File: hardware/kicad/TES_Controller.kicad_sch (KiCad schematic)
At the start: 81 parts, among them CN1 B2PS-VH(LF)(SN), CN2 S4B-XH-A(LF)(SN), CN3 DG381-3.5-02P-14-00A(H), CN5 DG381-3.5-02P-14-00A(H), CN6 DG381-3.5-02P-14-00A(H), Q1 AO3400A, Q2 AO3400A, Q3 AO3400A, Q4 AO3401A, U1 ESP32-S3-WROOM-1-N16R8, U10 DG301-5.0-02P-14-00A(H), U12 TJA1051T/3/1J, U5 ADS1115IDGSR, U6 AMS1117-3.3, U8 LMZM23601V5SILR

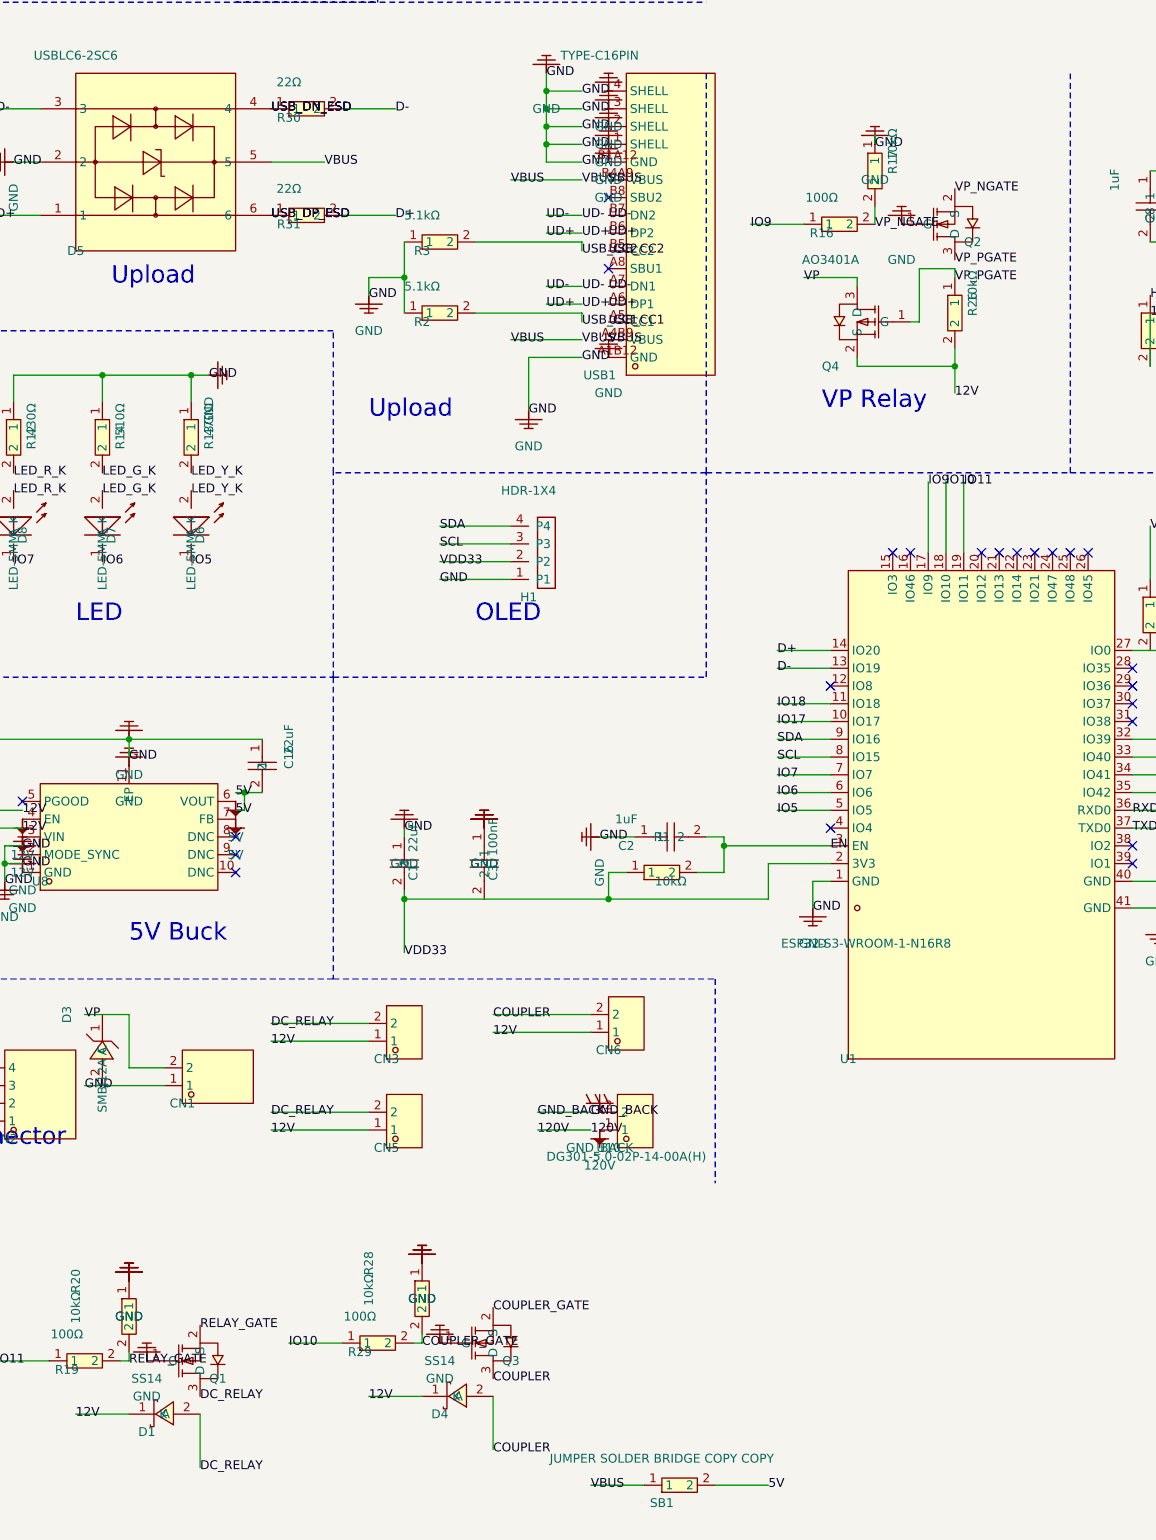
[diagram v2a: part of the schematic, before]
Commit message: Keep the AO3400A pin swap that the EasyEDA design relied on
LCSC's SOT-23-3 footprint for C20917 numbers pads 1 and 2 the opposite
way round from JEDEC TO-236: viewed from the top, 1 -> 2 -> 3 runs
clockwise, so the pad stamped "1" sits under the chip's pin 2. Every
other package in this library runs counter-clockwise, and each of those
checks out against its own datasheet — TJA1051 pin 1 is TXD, AMS1117
pin 1 is GND, USBLC6 pin 2 is GND, and Q4's AO3401A takes its gate on
pad 1 with an unmodified symbol.

The EasyEDA design compensated by drawing Q1-Q3 with a symbol whose
pins 1 and 2 are swapped, which is why the board works. The migration
dropped that: the generated library carries LCSC's own symbol with
pin 1 named G, so the schematic read "gate tied to GND" while the copper
underneath was right. Nothing in ERC or DRC objects to that, and the
failure on a built board is silent — the relay simply never closes.

tools/kicad_lib.py now reapplies the swap after every library
regeneration. The footprint and the PCB are untouched; CLAUDE.md records
the evidence and what the other half of the fix would cost if the
library is ever made to match the datasheet instead.

Side effect worth having: Q1-Q3's pins now line up with the original
drawing, so they keep their wires instead of falling back to labels —
12 components need label-only wiring now rather than 15, and 21 wire
segments are trimmed rather than 31.

Netlist still verifies at zero difference (230 of 230), ERC is clean,
PCB unchanged at 0 DRC errors and 0 unconnected pads.

Co-Authored-By: Claude Opus 5 <noreply@anthropic.com>
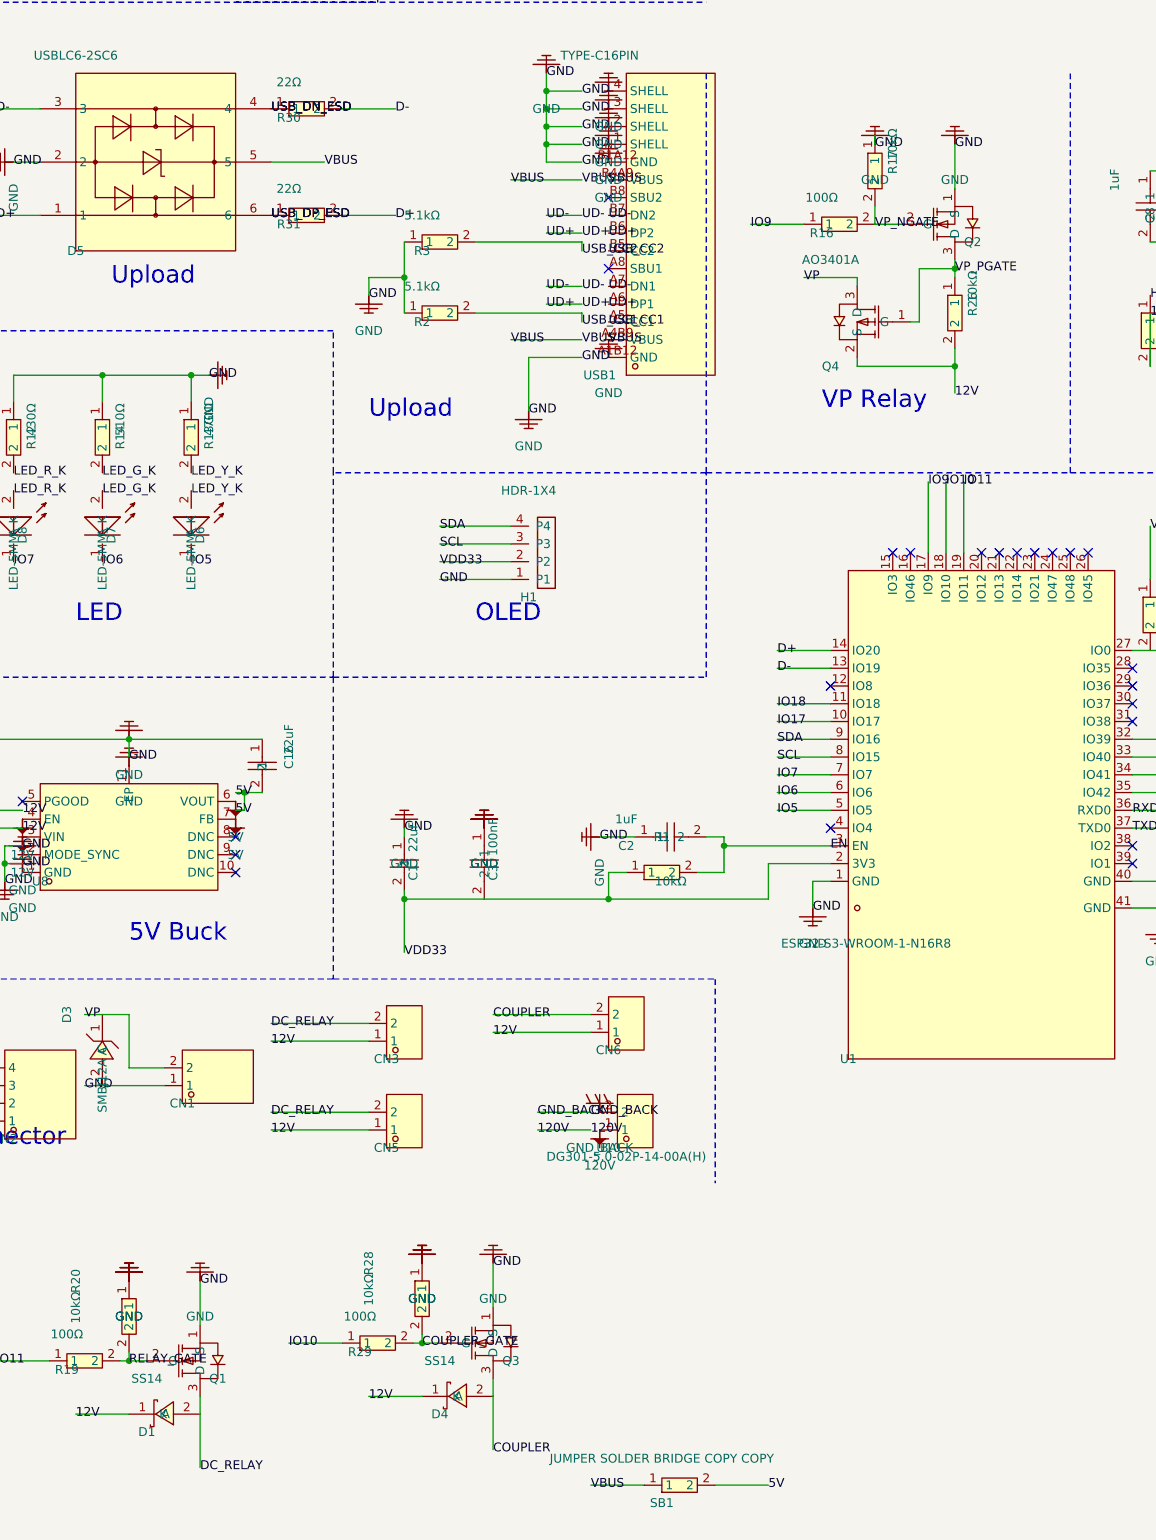
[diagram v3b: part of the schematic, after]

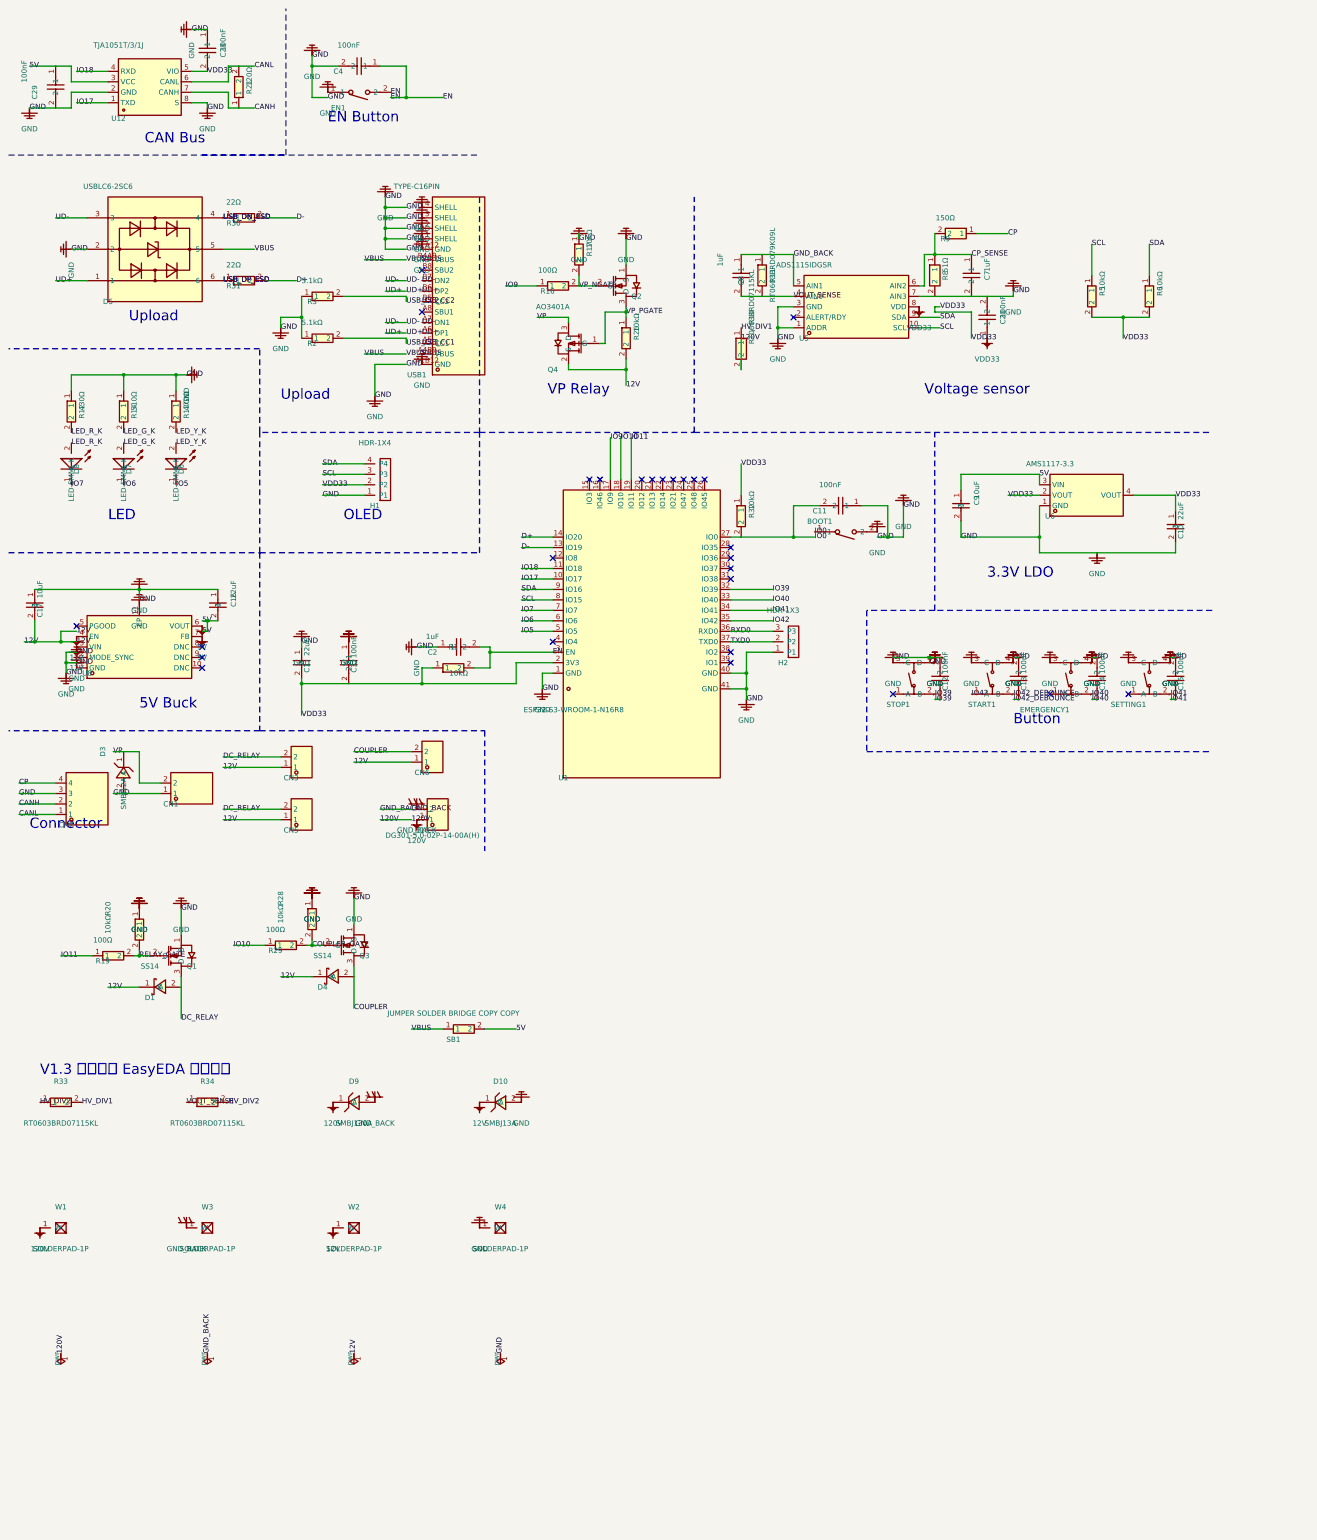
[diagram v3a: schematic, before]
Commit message: Record the V1.3 change set, and pause before it reaches the board
Three changes are decided and carried in the schematic and library; none of
them are on the PCB yet. Recording the split explicitly so the next session
does not mistake it for an unfinished edit:

* U13 24C02S EEPROM (LCSC C18723540) with C30 decoupling — stores the board
  revision so one binary can serve V1.3 and the 30.000-divider units in the
  field. WP to GND, firmware decides when to write.
* D10 becomes SMBJ12A, the part D3 already uses, and moves out from under the
  buck module. Lower clamp (19.9 V against 21.5 V) and no new part number.
* R35, a 10 k that divides Q4's gate drive. Q4 sat at exactly its ±12 V
  absolute-maximum V_GS whenever VP was on, and above it on a 12.6 V rail —
  which matches the field failures: rare, no external damage, fixed by
  replacement. Now −6 V.

The EEPROM cannot reach the PCB yet. Counting tracks and vias rather than only
component courtyards, the nearest free 4×4 mm to an SDA or SCL pad is 31.9 mm,
and 49.3 mm for enough room to escape three pins. Left alone the placer sends
SDA and SCL 28 mm each down the bottom layer, cutting the ground plane the
restructure work created. The board is therefore left at its last good state —
81 footprints, 0 DRC errors, 0 unconnected — rather than half-modified.

Two bugs found while doing this, both fixed and both older than this change:

* easyeda2kicad's --overwrite appends rather than replaces, so every library
  regeneration duplicated every symbol. 35 duplicates removed. The duplicate
  quietly reverted the AO3400A pin renumbering, leaving one symbol with 1=G and
  one with 1=S in the same library.
* The buck-module keepout was the rectangle through the four mounting holes
  rather than the module body, short by 2.4-3.0 mm on every edge. That is how
  D10 came to sit under the module in the first place.

Work stops here pending a decision on patent filing and a possible move to a
private repository. CLAUDE.md now car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
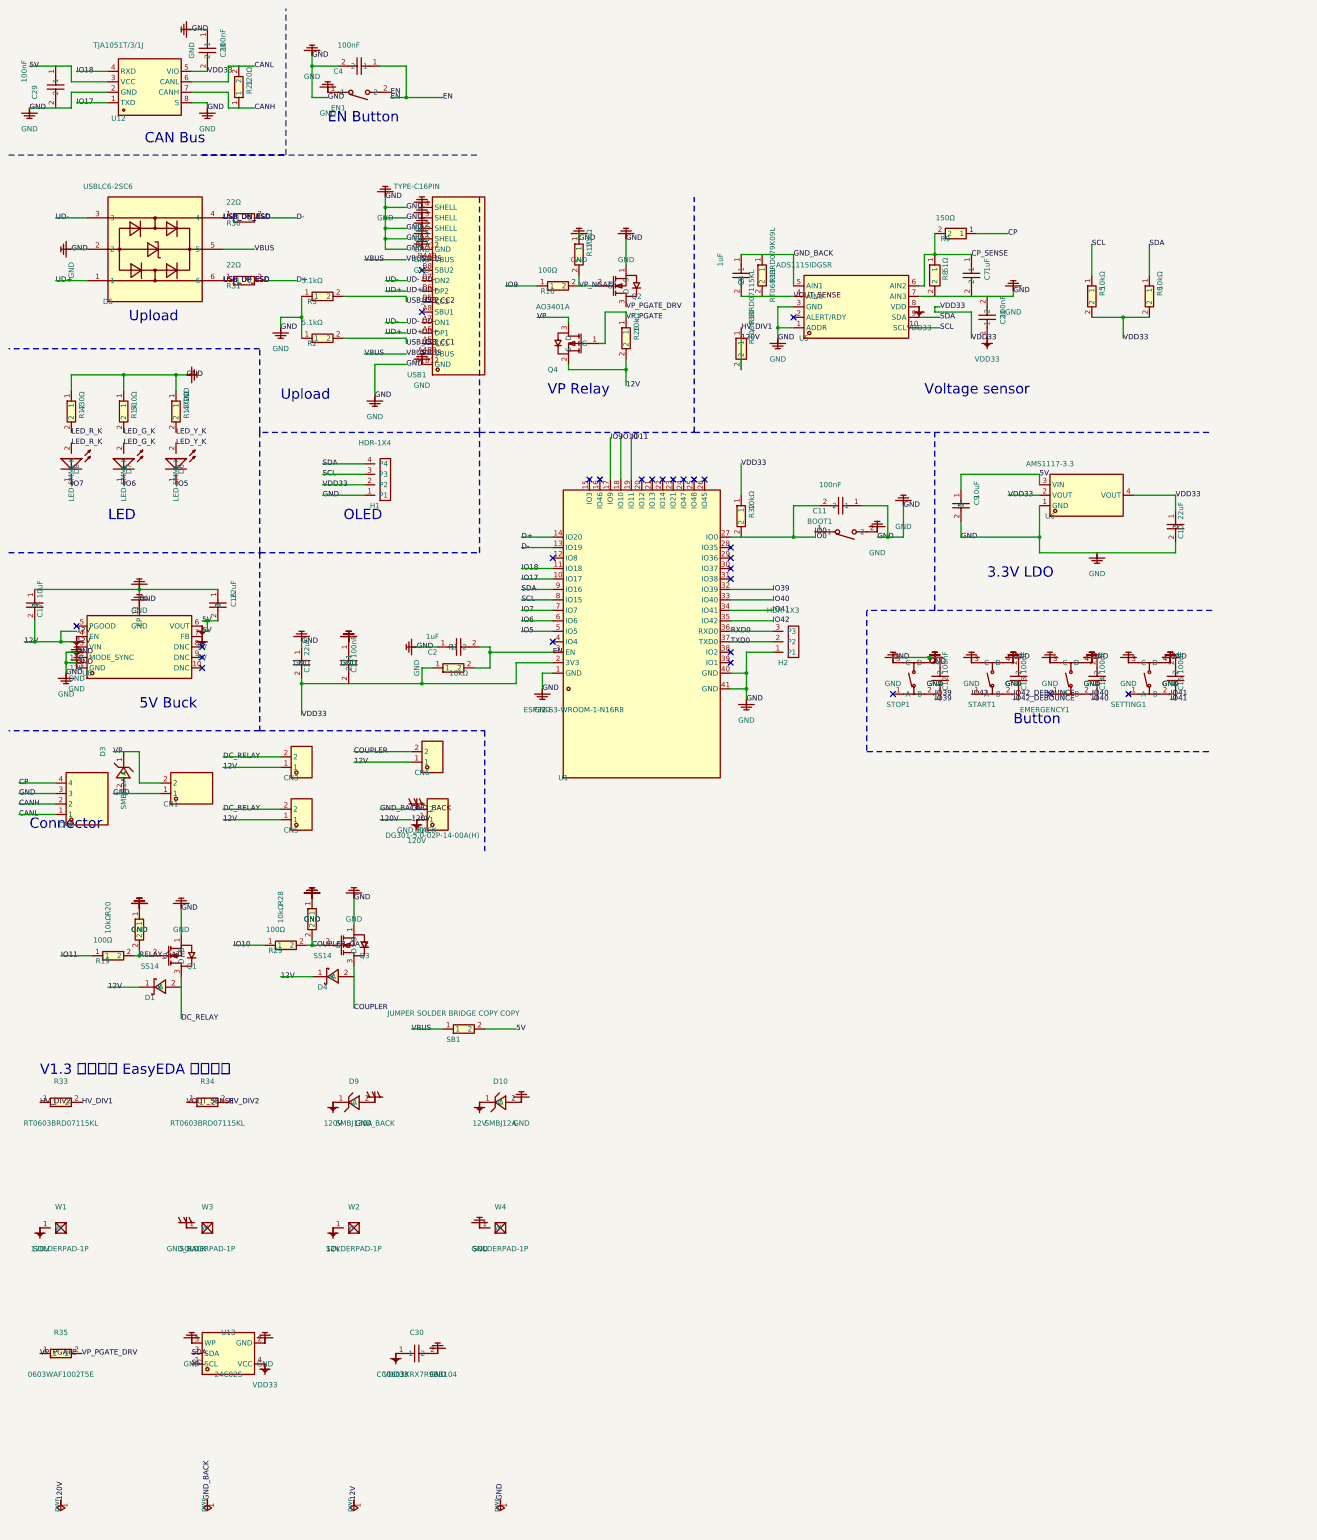
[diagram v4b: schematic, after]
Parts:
- added C30: CC0603KRX7R9BB104, TES:C0603, symbol TES:CC0603KRX7R9BB104
- added R35: 0603WAF1002T5E, TES:R0603, symbol TES:0603WAF1002T5E
- added U13: 24C02S, TES:SOT-23-5_L3.0-W1.6-P0.95-LS2.8-BR, symbol TES:24C02S
- D10: value SMBJ13A -> SMBJ12A
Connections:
- net GND: now also C30.2, U13.2 (GND), U13.5 (WP)
- net SCL: now also U13.1 (SCL)
- net SDA: now also U13.3 (SDA)
- net VDD33: now also C30.1, U13.4 (VCC)
- net VP_PGATE: now also R35.1; no longer Q2.3 (D)
- new net VP_PGATE_DRV: Q2.3 (D), R35.2
